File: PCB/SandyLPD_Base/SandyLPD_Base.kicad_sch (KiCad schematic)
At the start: 232 parts, among them J1 Conn_02x02_Odd_Even, J10 Conn_01x10_Pin, J11 Conn_01x03, J2 Conn_01x03, J4 Conn_01x10_Pin, J5 USB_C_Receptacle_USB2.0, J6 USB_C_Receptacle_USB2.0, J7 USB_C_Receptacle_USB2.0, J8 USB_C_Receptacle_USB2.0, J9 Conn_02x02_Odd_Even, SW1 BOOT_ALT, SW2 RESET_ALT, SW3 SW_DIP_x04, SW4 BOOT_ALT, SW5 RESET_ALT, SW6 SW_DIP_x04, U1 NCP1117-3.3_SOT223, U2 NCP1117-3.3_SOT223, U3 RP2040, U4 W25Q128JVPIQ, U5 RP2040, U6 W25Q128JVPIQ, Y1 12MHz, Y2 12MHz

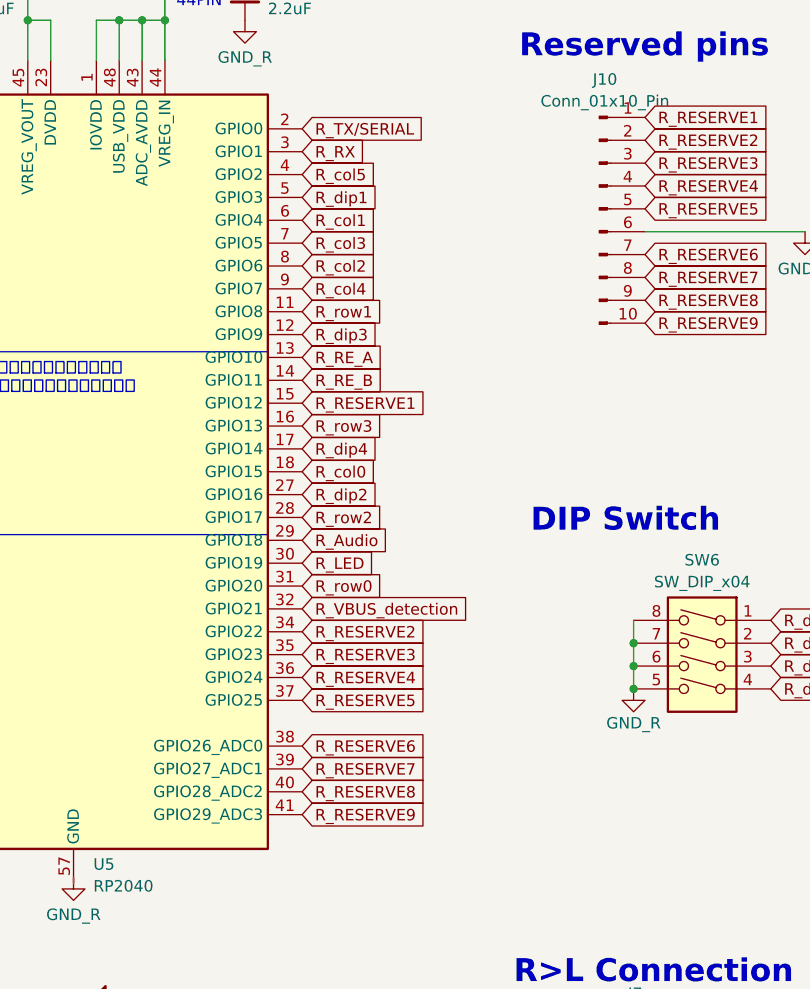
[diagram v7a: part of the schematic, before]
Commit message: 基板Base右手側　配線中
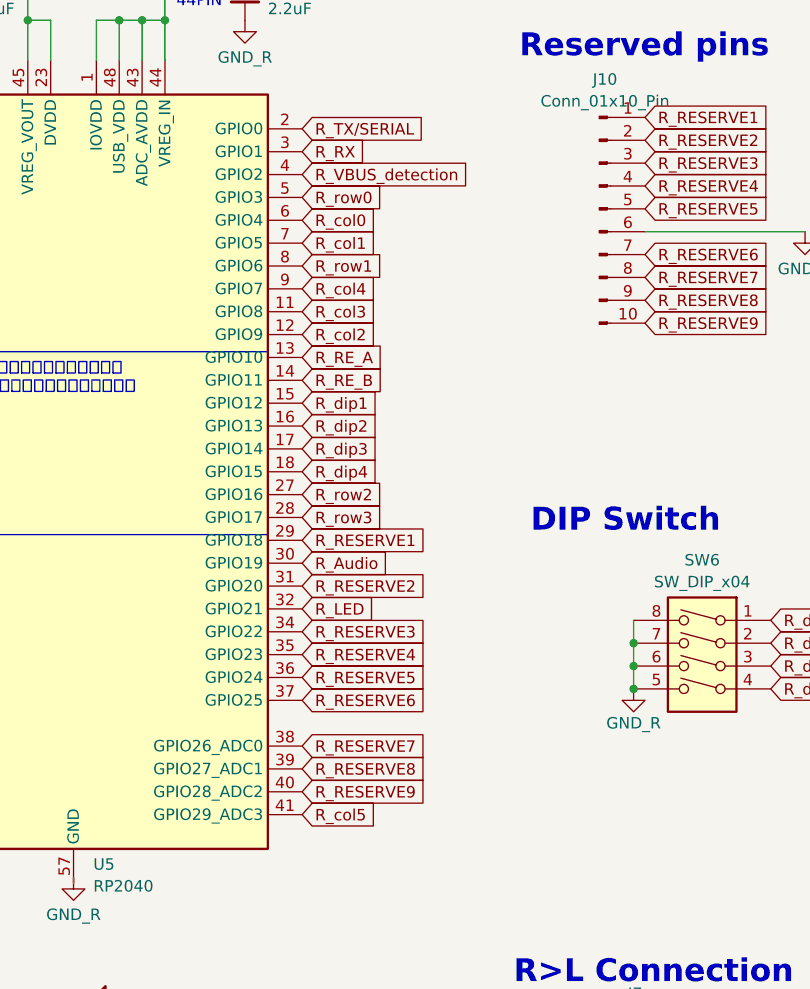
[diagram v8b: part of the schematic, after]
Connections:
- net R_Audio: now also U5.30 (GPIO19); no longer U5.29 (GPIO18)
- net R_LED: now also U5.32 (GPIO21); no longer U5.30 (GPIO19)
- net R_RESERVE1: now also U5.29 (GPIO18); no longer U5.15 (GPIO12)
- net R_RESERVE2: now also U5.31 (GPIO20); no longer U5.34 (GPIO22)
- net R_RESERVE3: now also U5.34 (GPIO22); no longer U5.35 (GPIO23)
- net R_RESERVE4: now also U5.35 (GPIO23); no longer U5.36 (GPIO24)
- net R_RESERVE5: now also U5.36 (GPIO24); no longer U5.37 (GPIO25)
- net R_RESERVE6: now also U5.37 (GPIO25); no longer U5.38 (GPIO26_ADC0)
- net R_RESERVE7: now also U5.38 (GPIO26_ADC0); no longer U5.39 (GPIO27_ADC1)
- net R_RESERVE8: now also U5.39 (GPIO27_ADC1); no longer U5.40 (GPIO28_ADC2)
- net R_RESERVE9: now also U5.40 (GPIO28_ADC2); no longer U5.41 (GPIO29_ADC3)
- net R_VBUS_detection: now also U5.4 (GPIO2); no longer U5.32 (GPIO21)
- net R_col0: now also U5.6 (GPIO4); no longer U5.18 (GPIO15)
- net R_col1: now also U5.7 (GPIO5); no longer U5.6 (GPIO4)
- net R_col2: now also U5.12 (GPIO9); no longer U5.8 (GPIO6)
- net R_col3: now also U5.11 (GPIO8); no longer U5.7 (GPIO5)
- net R_col5: now also U5.41 (GPIO29_ADC3); no longer U5.4 (GPIO2)
- net R_dip1: now also U5.15 (GPIO12); no longer U5.5 (GPIO3)
- net R_dip2: now also U5.16 (GPIO13); no longer U5.27 (GPIO16)
- net R_dip3: now also U5.17 (GPIO14); no longer U5.12 (GPIO9)
- net R_dip4: now also U5.18 (GPIO15); no longer U5.17 (GPIO14)
- net R_row0: now also U5.5 (GPIO3); no longer U5.31 (GPIO20)
- net R_row1: now also U5.8 (GPIO6); no longer U5.11 (GPIO8)
- net R_row2: now also U5.27 (GPIO16); no longer U5.28 (GPIO17)
- net R_row3: now also U5.28 (GPIO17); no longer U5.16 (GPIO13)
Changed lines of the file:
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@@
 	(global_label "R_RESERVE1"
 		(shape input)
-		(at 665.48 125.73 0)
+		(at 665.48 140.97 0)
 		(fields_autoplaced yes)
 		(effects
@@
 		)
 		(property "Intersheetrefs" "${INTERSHEET_REFS}"
-			(at 679.5432 125.73 0)
+			(at 679.5432 140.97 0)
 			(effects
 				(font
@@
 	(global_label "R_col3"
 		(shape input)
-		(at 665.48 107.95 0)
+		(at 665.48 115.57 0)
 		(fields_autoplaced yes)
 		(effects
@@
 		)
 		(property "Intersheetrefs" "${INTERSHEET_REFS}"
-			(at 674.1609 107.95 0)
+			(at 674.1609 115.57 0)
 			(effects
 				(font
@@
 		)
 		(property "シート間のリファレンス" "${INTERSHEET_REFS}"
-			(at 665.48 109.7852 0)
+			(at 665.48 117.4052 0)
 			(effects
 				(font
@@
 	(global_label "R_col1"
 		(shape input)
-		(at 665.48 105.41 0)
+		(at 665.48 107.95 0)
 		(fields_autoplaced yes)
 		(effects
@@
 		)
 		(property "Intersheetrefs" "${INTERSHEET_REFS}"
-			(at 674.1609 105.41 0)
+			(at 674.1609 107.95 0)
 			(effects
 				(font
@@
 		)
 		(property "シート間のリファレンス" "${INTERSHEET_REFS}"
-			(at 665.48 107.2452 0)
+			(at 665.48 109.7852 0)
 			(effects
 				(font
@@
 	(global_label "R_row3"
 		(shape input)
-		(at 665.48 128.27 0)
+		(at 665.48 138.43 0)
 		(fields_autoplaced yes)
 		(effects
@@
 		)
 		(property "Intersheetrefs" "${INTERSHEET_REFS}"
-			(at 674.5238 128.27 0)
+			(at 674.5238 138.43 0)
 			(effects
 				(font
@@
 		)
 		(property "シート間のリファレンス" "${INTERSHEET_REFS}"
-			(at 665.48 130.1052 0)
+			(at 665.48 140.2652 0)
 			(effects
 				(font
@@
 	(global_label "R_RESERVE7"
 		(shape input)
-		(at 665.48 166.37 0)
+		(at 665.48 163.83 0)
 		(fields_autoplaced yes)
 		(effects
@@
 		)
 		(property "Intersheetrefs" "${INTERSHEET_REFS}"
-			(at 679.5432 166.37 0)
+			(at 679.5432 163.83 0)
 			(effects
 				(font
@@
 	(global_label "R_dip3"
 		(shape input)
-		(at 665.48 118.11 0)
+		(at 665.48 130.81 0)
 		(fields_autoplaced yes)
 		(effects
@@
 		)
 		(property "Intersheetrefs" "${INTERSHEET_REFS}"
-			(at 674.1609 118.11 0)
+			(at 674.1609 130.81 0)
 			(effects
 				(font
@@
 	(global_label "R_row1"
 		(shape input)
-		(at 665.48 115.57 0)
+		(at 665.48 110.49 0)
 		(fields_autoplaced yes)
 		(effects
@@
 		)
 		(property "Intersheetrefs" "${INTERSHEET_REFS}"
-			(at 674.5238 115.57 0)
+			(at 674.5238 110.49 0)
 			(effects
 				(font
@@
 		)
 		(property "シート間のリファレンス" "${INTERSHEET_REFS}"
-			(at 665.48 117.4052 0)
+			(at 665.48 112.3252 0)
 			(effects
 				(font
@@
 	(global_label "R_dip1"
 		(shape input)
-		(at 665.48 102.87 0)
+		(at 665.48 125.73 0)
 		(fields_autoplaced yes)
 		(effects
@@
 		)
 		(property "Intersheetrefs" "${INTERSHEET_REFS}"
-			(at 674.1609 102.87 0)
+			(at 674.1609 125.73 0)
 			(effects
 				(font
@@
 	(global_label "R_RESERVE8"
 		(shape input)
-		(at 665.48 168.91 0)
+		(at 665.48 166.37 0)
 		(fields_autoplaced yes)
 		(effects
@@
 		)
 		(property "Intersheetrefs" "${INTERSHEET_REFS}"
-			(at 679.5432 168.91 0)
+			(at 679.5432 166.37 0)
 			(effects
 				(font
@@
 	(global_label "R_col2"
 		(shape input)
-		(at 665.48 110.49 0)
+		(at 665.48 118.11 0)
 		(fields_autoplaced yes)
 		(effects
@@
 		)
 		(property "Intersheetrefs" "${INTERSHEET_REFS}"
-			(at 674.1609 110.49 0)
+			(at 674.1609 118.11 0)
 			(effects
 				(font
@@
 		)
 		(property "シート間のリファレンス" "${INTERSHEET_REFS}"
-			(at 665.48 112.3252 0)
+			(at 665.48 119.9452 0)
 			(effects
 				(font
@@
 	(global_label "R_Audio"
 		(shape input)
-		(at 665.48 140.97 0)
+		(at 665.48 143.51 0)
 		(fields_autoplaced yes)
 		(effects
@@
 		)
 		(property "Intersheetrefs" "${INTERSHEET_REFS}"
-			(at 675.189 140.97 0)
+			(at 675.189 143.51 0)
 			(effects
 				(font
@@
 	(global_label "R_col0"
 		(shape input)
-		(at 665.48 133.35 0)
+		(at 665.48 105.41 0)
 		(fields_autoplaced yes)
 		(effects
@@
 		)
 		(property "Intersheetrefs" "${INTERSHEET_REFS}"
-			(at 674.1609 133.35 0)
+			(at 674.1609 105.41 0)
 			(effects
 				(font
@@
 		)
 		(property "シート間のリファレンス" "${INTERSHEET_REFS}"
-			(at 665.48 135.1852 0)
+			(at 665.48 107.2452 0)
 			(effects
 				(font
@@
 	(global_label "R_RESERVE5"
 		(shape input)
-		(at 665.48 158.75 0)
+		(at 665.48 156.21 0)
 		(fields_autoplaced yes)
 		(effects
@@
 		)
 		(property "Intersheetrefs" "${INTERSHEET_REFS}"
-			(at 679.5432 158.75 0)
+			(at 679.5432 156.21 0)
 			(effects
 				(font
@@
 	(global_label "R_RESERVE6"
 		(shape input)
-		(at 665.48 163.83 0)
+		(at 665.48 158.75 0)
 		(fields_autoplaced yes)
 		(effects
@@
 		)
 		(property "Intersheetrefs" "${INTERSHEET_REFS}"
-			(at 679.5432 163.83 0)
+			(at 679.5432 158.75 0)
 			(effects
 				(font
@@
 	(global_label "R_dip4"
 		(shape input)
-		(at 665.48 130.81 0)
+		(at 665.48 133.35 0)
 		(fields_autoplaced yes)
 		(effects
@@
 		)
 		(property "Intersheetrefs" "${INTERSHEET_REFS}"
-			(at 674.1609 130.81 0)
+			(at 674.1609 133.35 0)
 			(effects
 				(font
@@
 	(global_label "R_RESERVE4"
 		(shape input)
-		(at 665.48 156.21 0)
+		(at 665.48 153.67 0)
 		(fields_autoplaced yes)
 		(effects
@@
 		)
 		(property "Intersheetrefs" "${INTERSHEET_REFS}"
-			(at 679.5432 156.21 0)
+			(at 679.5432 153.67 0)
 			(effects
 				(font
@@
 	(global_label "R_RESERVE3"
 		(shape input)
-		(at 665.48 153.67 0)
+		(at 665.48 151.13 0)
 		(fields_autoplaced yes)
 		(effects
@@
 		)
 		(property "Intersheetrefs" "${INTERSHEET_REFS}"
-			(at 679.5432 153.67 0)
+			(at 679.5432 151.13 0)
 			(effects
 				(font
@@
 	(global_label "R_RESERVE2"
 		(shape input)
-		(at 665.48 151.13 0)
+		(at 665.48 146.05 0)
 		(fields_autoplaced yes)
 		(effects
@@
 		)
 		(property "Intersheetrefs" "${INTERSHEET_REFS}"
-			(at 679.5432 151.13 0)
+			(at 679.5432 146.05 0)
 			(effects
 				(font
@@
 	(global_label "R_RESERVE9"
 		(shape input)
-		(at 665.48 171.45 0)
+		(at 665.48 168.91 0)
 		(fields_autoplaced yes)
 		(effects
@@
 		)
 		(property "Intersheetrefs" "${INTERSHEET_REFS}"
-			(at 679.5432 171.45 0)
+			(at 679.5432 168.91 0)
 			(effects
 				(font
@@
 	(global_label "R_VBUS_detection"
 		(shape input)
-		(at 665.48 148.59 0)
+		(at 665.48 100.33 0)
 		(fields_autoplaced yes)
 		(effects
@@
 		)
 		(property "Intersheetrefs" "${INTERSHEET_REFS}"
-			(at 684.6838 148.59 0)
+			(at 684.6838 100.33 0)
 			(effects
 				(font
@@
 	(global_label "R_row2"
 		(shape input)
-		(at 665.48 138.43 0)
+		(at 665.48 135.89 0)
 		(fields_autoplaced yes)
 		(effects
@@
 		)
 		(property "Intersheetrefs" "${INTERSHEET_REFS}"
-			(at 674.5238 138.43 0)
+			(at 674.5238 135.89 0)
 			(effects
 				(font
@@
 		)
 		(property "シート間のリファレンス" "${INTERSHEET_REFS}"
-			(at 665.48 140.2652 0)
+			(at 665.48 137.7252 0)
 			(effects
 				(font
@@
 	(global_label "R_LED"
 		(shape input)
-		(at 665.48 143.51 0)
+		(at 665.48 148.59 0)
 		(fields_autoplaced yes)
 		(effects
@@
 		)
 		(property "Intersheetrefs" "${INTERSHEET_REFS}"
-			(at 673.4957 143.51 0)
+			(at 673.4957 148.59 0)
 			(effects
 				(font
@@
 		)
 		(property "シート間のリファレンス" "${INTERSHEET_REFS}"
-			(at 665.48 145.3452 0)
+			(at 665.48 150.4252 0)
 			(effects
 				(font
@@
 	(global_label "R_row0"
 		(shape input)
-		(at 665.48 146.05 0)
+		(at 665.48 102.87 0)
 		(fields_autoplaced yes)
 		(effects
@@
 		)
 		(property "Intersheetrefs" "${INTERSHEET_REFS}"
-			(at 674.5238 146.05 0)
+			(at 674.5238 102.87 0)
 			(effects
 				(font
@@
 		)
 		(property "シート間のリファレンス" "${INTERSHEET_REFS}"
-			(at 665.48 147.8852 0)
+			(at 665.48 104.7052 0)
 			(effects
 				(font
@@
 	(global_label "R_dip2"
 		(shape input)
-		(at 665.48 135.89 0)
+		(at 665.48 128.27 0)
 		(fields_autoplaced yes)
 		(effects
@@
 		)
 		(property "Intersheetrefs" "${INTERSHEET_REFS}"
-			(at 674.1609 135.89 0)
+			(at 674.1609 128.27 0)
 			(effects
 				(font
@@
 	(global_label "R_col5"
 		(shape input)
-		(at 665.48 100.33 0)
+		(at 665.48 171.45 0)
 		(fields_autoplaced yes)
 		(effects
@@
 		)
 		(property "Intersheetrefs" "${INTERSHEET_REFS}"
-			(at 674.1609 100.33 0)
+			(at 674.1609 171.45 0)
 			(effects
 				(font
@@
 		)
 		(property "シート間のリファレンス" "${INTERSHEET_REFS}"
-			(at 665.48 102.1652 0)
+			(at 665.48 173.2852 0)
 			(effects
 				(font
